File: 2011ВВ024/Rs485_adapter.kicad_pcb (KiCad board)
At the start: 2 copper layers, 31.5 x 13 mm, 9 parts

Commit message: Резонит плакал
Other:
- board size 31.5 x 13 mm -> 31 x 13 mm
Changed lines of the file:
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@@
-(kicad_pcb (version 20171130) (host pcbnew "(5.0.0)")
+(kicad_pcb (version 20171130) (host pcbnew "(5.0.2)-1")
   (general
     (thickness 1.6)
@@
       (creategerberjobfile false)
       (excludeedgelayer true)
-      (linewidth 0.200000)
+      (linewidth 0.100000)
       (plotframeref false)
       (viasonmask false)
@@
     (effects (font (size 1.5 1.5) (thickness 0.3)))
   )
-  (gr_line (start 134.25 84.5) (end 134.25 97.5) (layer Edge.Cuts) (width 0.15))
-  (gr_line (start 165.75 97.5) (end 165.75 84.5) (layer Edge.Cuts) (width 0.15))
-  (gr_line (start 165.75 84.5) (end 134.25 84.5) (layer Edge.Cuts) (width 0.15))
-  (gr_line (start 134.25 97.5) (end 165.75 97.5) (layer Edge.Cuts) (width 0.15))
+  (gr_line (start 134.5 84.5) (end 134.5 97.5) (layer Edge.Cuts) (width 0.15))
+  (gr_line (start 165.5 97.5) (end 165.5 84.5) (layer Edge.Cuts) (width 0.15))
+  (gr_line (start 165.5 84.5) (end 134.5 84.5) (layer Edge.Cuts) (width 0.15))
+  (gr_line (start 134.5 97.5) (end 165.5 97.5) (layer Edge.Cuts) (width 0.15))
   (gr_text o (at 149.5 88) (layer F.Cu)
     (effects (font (size 1.5 1.5) (thickness 0.3)))

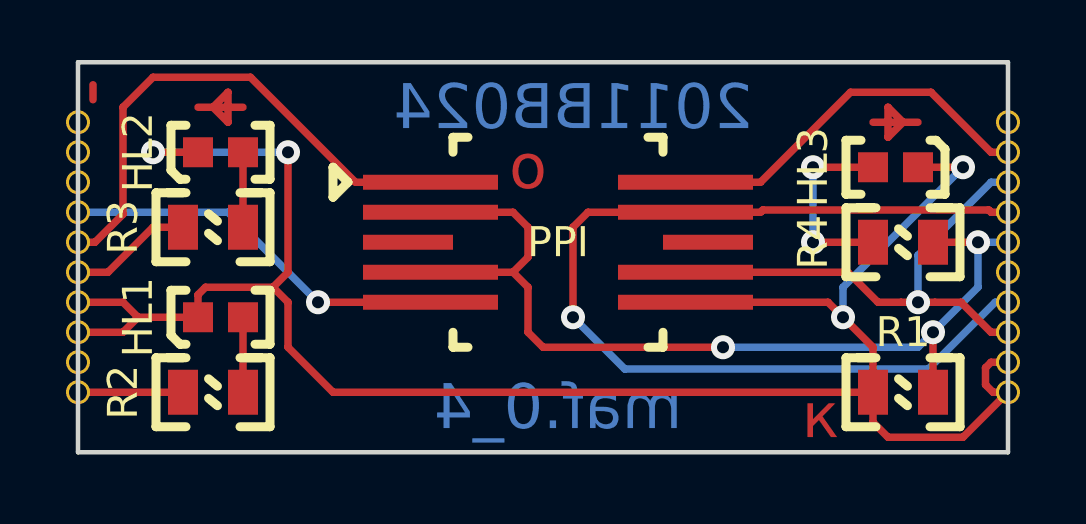
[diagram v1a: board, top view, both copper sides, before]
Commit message: увеличены зазоры и квадратизированы площадки
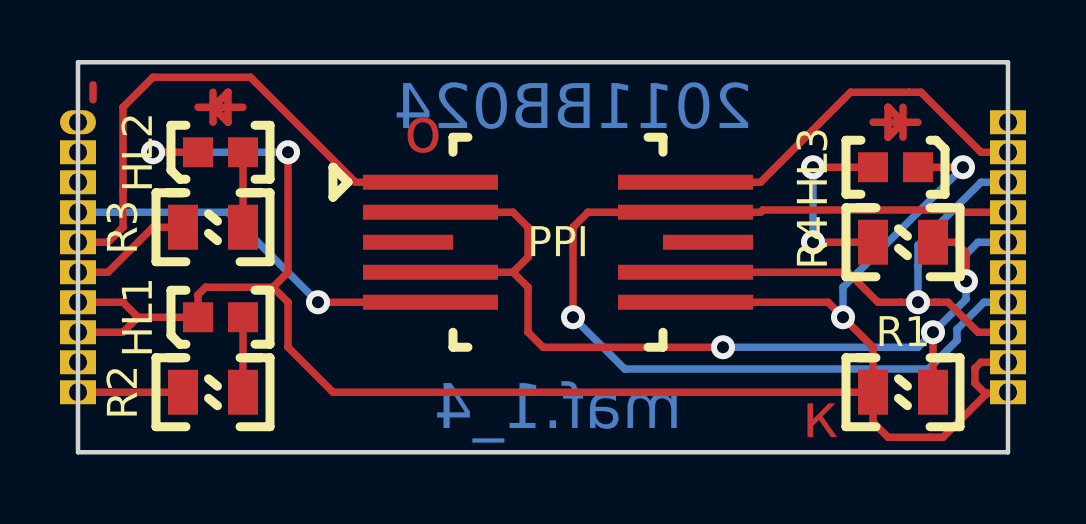
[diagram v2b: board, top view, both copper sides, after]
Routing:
- net (no net): track 8.33 -> 10.3 mm
- net Net-(A1-Pad1B): track 67.9 -> 67.1 mm
- net Net-(A1-Pad3B): track 17.2 -> 16.5 mm
- net Net-(A1-Pad4B): track 33.9 -> 33.3 mm
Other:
- board text added: "maf.1_4"
- board text removed: "maf.0_4"
